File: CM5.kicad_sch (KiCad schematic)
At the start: 4 parts, among them J301 Conn_01x03, M303 Compute-Module-4_H1.5mm

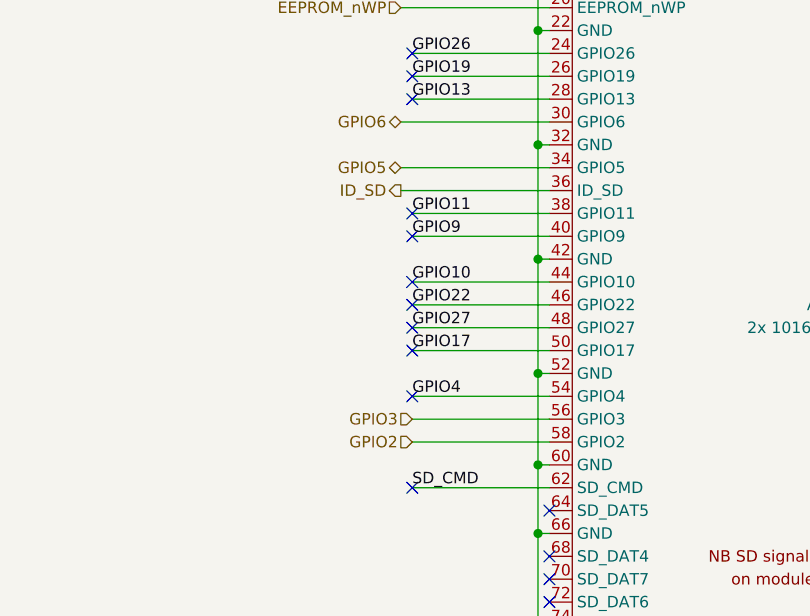
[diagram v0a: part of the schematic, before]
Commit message: RAK3172 from UART0_IR to UART3
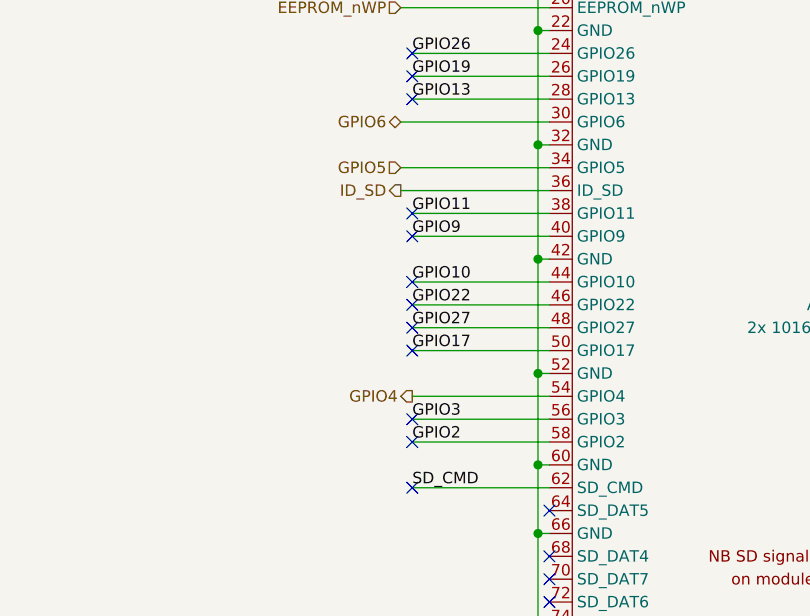
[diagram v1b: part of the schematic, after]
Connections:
- no-connect marks 94 -> 95
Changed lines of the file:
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@@
 	)
 	(no_connect
-		(at 71.12 144.78)
+		(at 71.12 149.86)
 	)
 	(no_connect
@@
 	)
 	(no_connect
+		(at 71.12 147.32)
+	)
+	(no_connect
 		(at 345.44 132.08)
 	)
@@
 		)
 	)
+	(label "GPIO2"
+		(at 71.12 149.86 0)
+		(fields_autoplaced yes)
+		(effects
+			(font
+				(size 1.27 1.27)
+			)
+			(justify left bottom)
+		)
+	)
 	(label "GPIO11"
 		(at 71.12 124.46 0)
@@
 		)
 	)
+	(label "GPIO3"
+		(at 71.12 147.32 0)
+		(fields_autoplaced yes)
+		(effects
+			(font
+				(size 1.27 1.27)
+			)
+			(justify left bottom)
+		)
+	)
 	(label "DPHY1_D1_N"
 		(at 344.805 182.88 180)
@@
 		)
 	)
-	(label "GPIO4"
-		(at 71.12 144.78 0)
-		(fields_autoplaced yes)
-		(effects
-			(font
-				(size 1.27 1.27)
-			)
-			(justify left bottom)
-		)
-	)
 	(label "PCIE_nRST"
 		(at 345.44 91.44 180)
@@
 	)
 	(hierarchical_label "GPIO5"
-		(shape bidirectional)
+		(shape input)
 		(at 69.85 119.38 180)
 		(fields_autoplaced yes)
@@
 		)
 	)
-	(hierarchical_label "GPIO3"
+	(hierarchical_label "+5V"
 		(shape input)
-		(at 71.12 147.32 180)
+		(at 163.83 175.26 0)
 		(fields_autoplaced yes)
 		(effects
@@
 				(size 1.27 1.27)
 			)
-			(justify right)
+			(justify left)
 		)
 	)
-	(hierarchical_label "GPIO2"
-		(shape input)
-		(at 71.12 149.86 180)
+	(hierarchical_label "1V8_CM4"
+		(shape output)
+		(at 69.85 187.96 180)
 		(fields_autoplaced yes)
 		(effects
@@
 		)
 	)
-	(hierarchical_label "+5V"
-		(shape input)
-		(at 163.83 175.26 0)
-		(fields_autoplaced yes)
-		(effects
-			(font
-				(size 1.27 1.27)
-			)
-			(justify left)
-		)
-	)
-	(hierarchical_label "1V8_CM4"
+	(hierarchical_label "GPIO4"
 		(shape output)
-		(at 69.85 187.96 180)
+		(at 71.12 144.78 180)
 		(fields_autoplaced yes)
 		(effects
